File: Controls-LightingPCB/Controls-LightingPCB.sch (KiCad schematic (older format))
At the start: 19 parts, among them J1 Conn_01x11

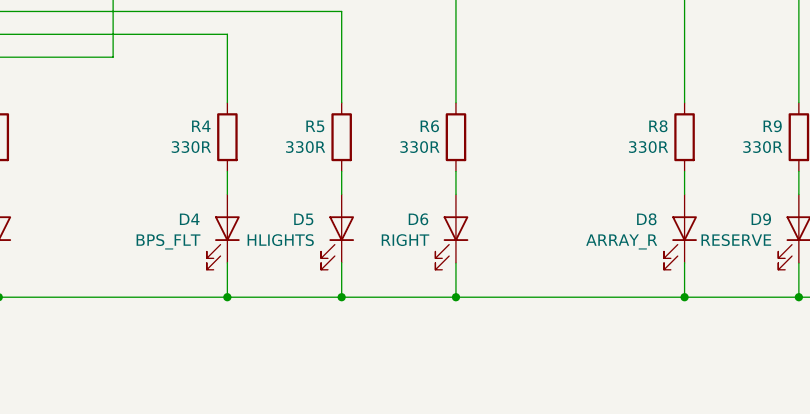
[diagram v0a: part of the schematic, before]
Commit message: Finished PCB layout
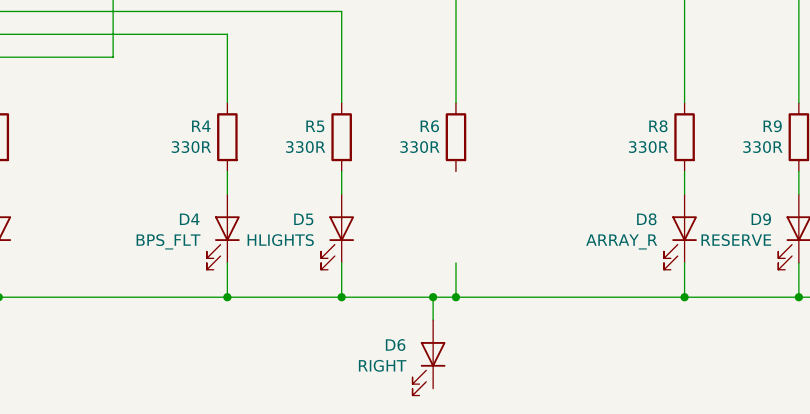
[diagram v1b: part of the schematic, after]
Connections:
- wire segments 51 -> 52
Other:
- moved on the sheet: D6
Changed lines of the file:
@@
 L Device:LED D6
 U 1 1 5F66A48A
-P 5000 3550
-F 0 "D6" V 5039 3433 50  0000 R CNN
-F 1 "RIGHT" V 4948 3433 50  0000 R CNN
-F 2 "Diode_SMD:D_0805_2012Metric" H 5000 3550 50  0001 C CNN
-F 3 "~" H 5000 3550 50  0001 C CNN
-	1    5000 3550
+P 4900 4100
+F 0 "D6" V 4939 3983 50  0000 R CNN
+F 1 "RIGHT" V 4848 3983 50  0000 R CNN
+F 2 "Diode_SMD:D_0805_2012Metric" H 4900 4100 50  0001 C CNN
+F 3 "~" H 4900 4100 50  0001 C CNN
+	1    4900 4100
 	0    1    -1   0
 $EndComp
@@
 	5500 1600 5500 1700
 Wire Wire Line
-	5000 3300 5000 3400
+	4900 3850 4900 3950
 Wire Wire Line
 	4500 3300 4500 3400
@@
 	5000 3700 5000 3850
 Wire Wire Line
-	5000 3850 4500 3850
+	5000 3850 4900 3850
 Connection ~ 4500 3850
 Wire Wire Line
@@
 Wire Wire Line
 	3500 1200 2500 1200
+Connection ~ 4900 3850
+Wire Wire Line
+	4900 3850 4500 3850
 $EndSCHEMATC

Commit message: Added hierarchical sheets and connections
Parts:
- removed D10: MOTOR, Diode_SMD:D_0805_2012Metric, symbol Device:LED
- removed D2: BPS_R, Diode_SMD:D_0805_2012Metric, symbol Device:LED
- removed D3: LEFT, Diode_SMD:D_0805_2012Metric, symbol Device:LED
- removed D4: BPS_FLT, Diode_SMD:D_0805_2012Metric, symbol Device:LED
- removed D5: HLIGHTS, Diode_SMD:D_0805_2012Metric, symbol Device:LED
- removed D6: RIGHT, Diode_SMD:D_0805_2012Metric, symbol Device:LED
- removed D7: CTRL_FLT, Diode_SMD:D_0805_2012Metric, symbol Device:LED
- removed D8: ARRAY_R, Diode_SMD:D_0805_2012Metric, symbol Device:LED
- removed D9: RESERVE, Diode_SMD:D_0805_2012Metric, symbol Device:LED
- removed J1: Conn_01x11, Connector_PinHeader_2.54mm:PinHeader_1x11_P2.54mm_Vertical, symbol Connector_Generic:Conn_01x11
- removed R10, R3, R4, R5, R6, R7, R8, R9: 330R, Resistor_SMD:R_0805_2012Metric, symbol Device:R
- removed R2: 1.2k, Resistor_SMD:R_0805_2012Metric, symbol Device:R
- added J?: Conn_02x06_Counter_Clockwise, symbol Connector_Generic:Conn_02x06_Counter_Clockwise
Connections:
- net labels removed: +3.3V, GNDPWR
- wire segments 52 -> 16
